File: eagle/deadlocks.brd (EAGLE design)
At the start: 78.7 x 93.3 mm, 18 parts, among them J1 6_PIN_SERIAL_CABLEPTH, U1 328P

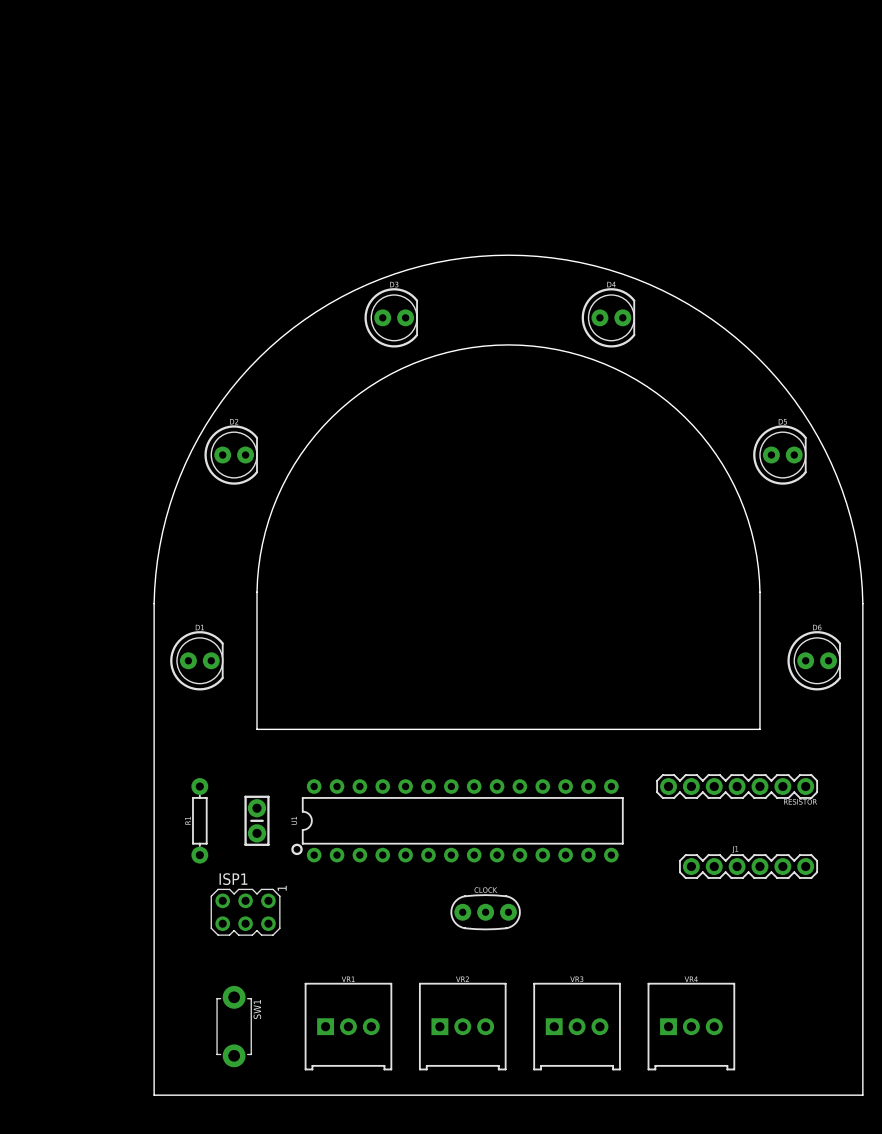
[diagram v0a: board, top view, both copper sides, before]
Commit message: Cleaned up outdated designs and gerbers
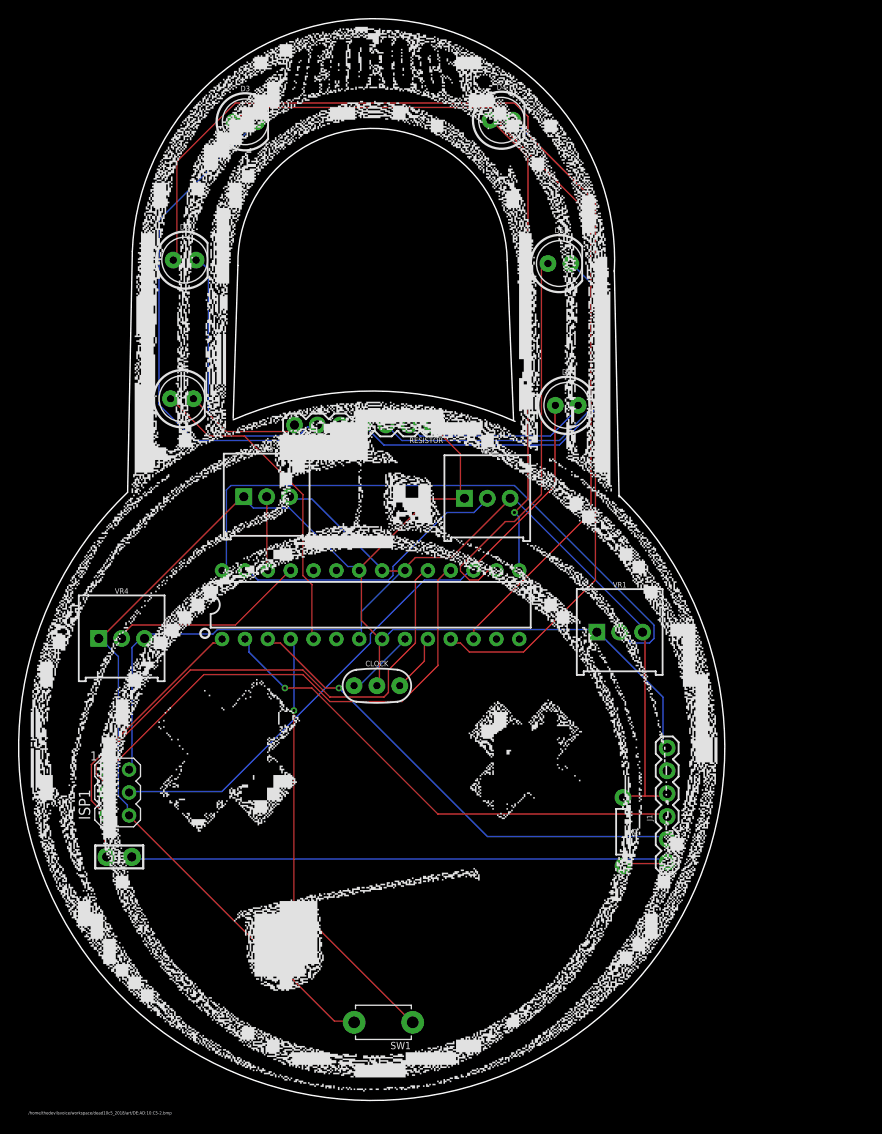
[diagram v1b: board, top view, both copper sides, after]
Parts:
- moved VR4 76.6 mm to (10.4, 52.0)
- moved VR3 68.2 mm to (26.5, 67.8)
- moved VR2 58.8 mm to (51.0, 67.6)
- moved RESISTOR 57.8 mm to (44.8, 75.7)
- moved VR1 53.2 mm to (65.7, 52.7)
- moved R1 47.0 mm to (66.1, 30.5), turned to 270 degrees
- moved D6 39.7 mm to (59.8, 77.9)
- moved D5 32.7 mm to (59.0, 93.7)
- moved D1 29.2 mm to (17.1, 78.6)
- moved CLOCK 27.9 mm to (38.7, 46.8)
- moved D3 27.4 mm to (24.1, 109.4)
- moved U1 26.1 mm to (38.0, 55.8)
- moved D4 25.1 mm to (52.6, 109.6)
- moved D2 22.3 mm to (17.4, 94.0)
- moved ISP1 19.5 mm to (9.91, 34.9), turned to 0 degrees
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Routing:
- net GND: track 0.00 -> 174.4 mm
- net N$20: track 0.00 -> 128.2 mm
- net VCC: track 0.00 -> 126.4 mm
- net N$21: track 0.00 -> 98.6 mm
- net N$18: track 0.00 -> 71.1 mm
- net N$1: track 0.00 -> 69.3 mm
- net N$10: track 0.00 -> 64.8 mm
- net N$14: track 0.00 -> 64.3 mm
- net N$15: track 0.00 -> 58.4 mm
- net N$24: track 0.00 -> 57.4 mm
- net N$8: track 0.00 -> 55.6 mm, vias 0 -> 1
- net N$9: track 0.00 -> 55.4 mm
- net N$7: track 0.00 -> 53.6 mm, vias 0 -> 1
- net N$22: track 0.00 -> 52.6 mm, vias 0 -> 1
- net N$25: track 0.00 -> 48.2 mm, vias 0 -> 1
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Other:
- board size 78.7 x 93.3 mm -> 78.4 x 120.2 mm
- board text added: "/home/thedevilsvoice/workspace/dead10c5_2018/art/DE:AD:10:C5-2.bmp"
- board text added: "@DEAD10C5 DEFCON 26 #Badgelife"
- board text added: "@TheDevilsVoice @mzbat @p0lr_"

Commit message: Re-arranged components, added a power input, and fixed the gerbers so Seeed can manufacture the prototypes.
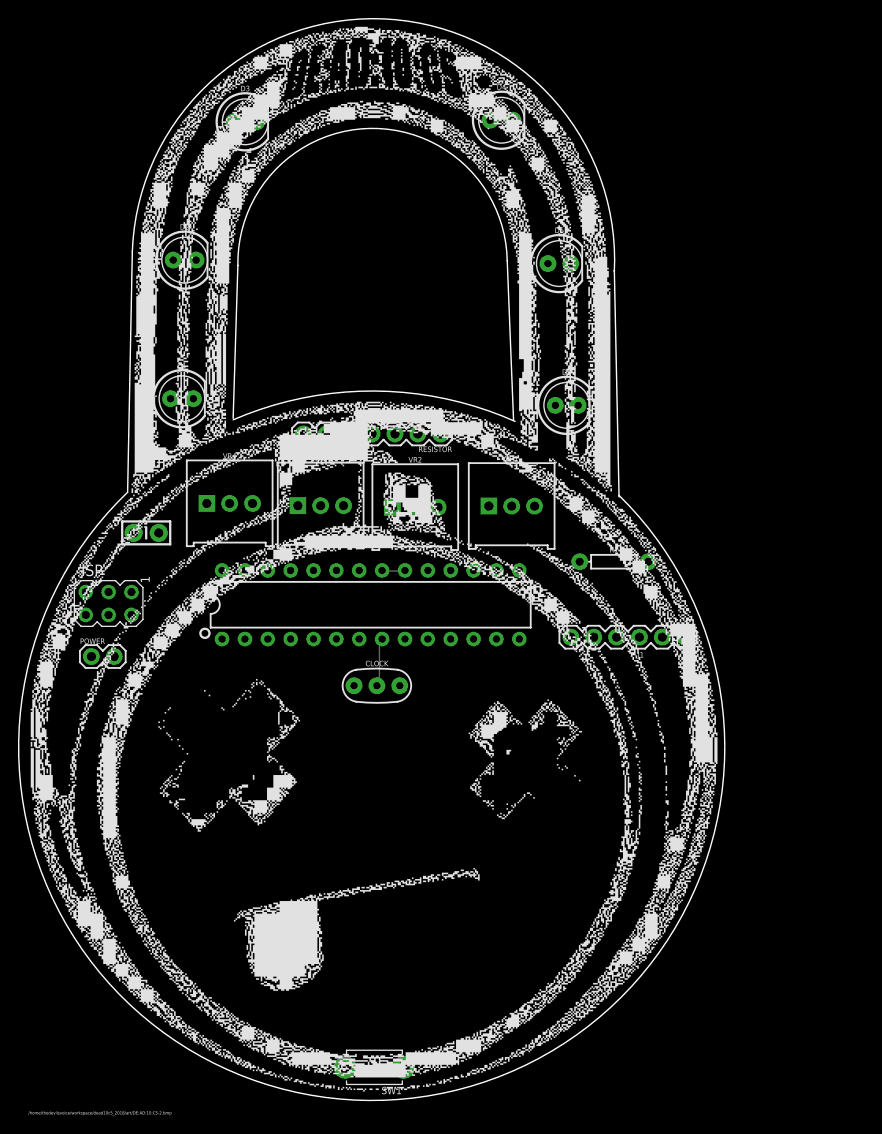
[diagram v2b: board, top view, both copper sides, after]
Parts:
- removed ISP1: AVRISP-6, adafruit:AVRISP
- added ISP: AVRISP-6, adafruit:AVRISP
- added POWER: (no value), SparkFun-Connectors:1X02
- moved C3 36.1 mm to (13.1, 63.7)
- moved R1 30.0 mm to (65.1, 60.5), turned to 0 degrees
- moved J1 25.1 mm to (73.0, 52.1), turned to 180 degrees
- moved VR4 19.2 mm to (22.4, 67.0)
- moved VR1 18.4 mm to (53.7, 66.7)
- moved VR2 8.06 mm to (43.0, 66.6)
- moved VR3 6.08 mm to (32.5, 66.8)
- moved SW1 5.10 mm to (38.4, 4.36)
- moved RESISTOR 1.41 mm to (45.8, 74.7)
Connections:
- net GND: now also ISP.6, POWER.2; no longer ISP1.6
- net N$11: now also ISP.5; no longer ISP1.5
- net N$18: now also ISP.4; no longer ISP1.4
- net N$24: now also ISP.3; no longer ISP1.3
- net N$9: now also ISP.1; no longer ISP1.1
- net VCC: now also ISP.2, POWER.1; no longer ISP1.2
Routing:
- net GND: track 174.4 -> 5.41 mm
- net N$20: track 128.2 -> 0.00 mm
- net VCC: track 126.4 -> 2.56 mm
- net N$21: track 98.6 -> 0.00 mm
- net N$18: track 71.1 -> 0.00 mm
- net N$1: track 69.3 -> 0.00 mm
- net N$10: track 64.8 -> 0.00 mm
- net N$14: track 64.3 -> 0.00 mm
- net N$15: track 58.4 -> 0.00 mm
- net N$24: track 57.4 -> 0.00 mm
- net N$8: track 55.6 -> 0.00 mm, vias 1 -> 0
- net N$9: track 55.4 -> 0.00 mm
- net N$7: track 53.6 -> 0.00 mm, vias 1 -> 0
- net N$22: track 52.6 -> 0.00 mm, vias 1 -> 0
- net N$25: track 48.2 -> 0.00 mm, vias 1 -> 0
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
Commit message: Forgot traces in the last version.
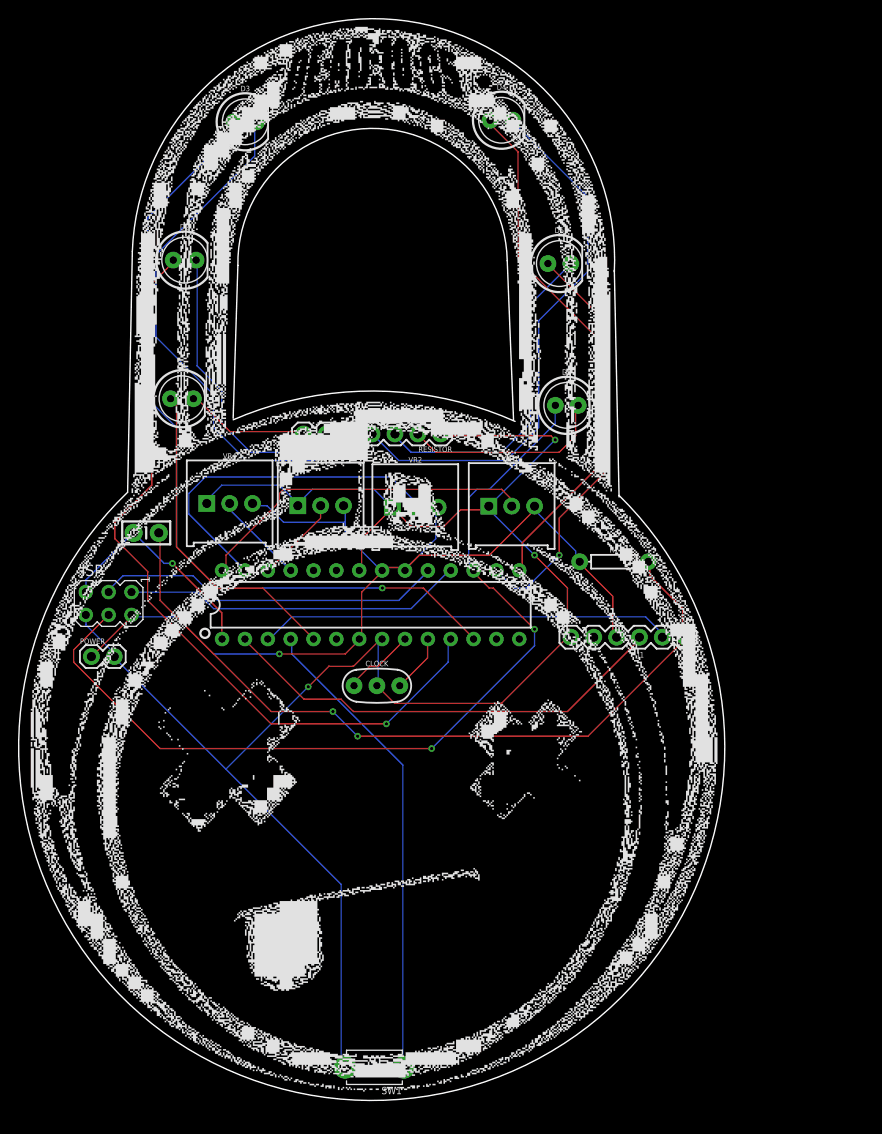
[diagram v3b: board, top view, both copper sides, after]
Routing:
- net GND: track 5.41 -> 204.5 mm, vias 0 -> 3
- net VCC: track 2.56 -> 111.4 mm, vias 0 -> 1
- net N$18: track 0.00 -> 101.6 mm, vias 0 -> 2
- net N$21: track 0.00 -> 89.9 mm, vias 0 -> 1
- net N$10: track 0.00 -> 87.1 mm, vias 0 -> 2
- net N$20: track 0.00 -> 86.6 mm, vias 0 -> 1
- net N$14: track 0.00 -> 61.1 mm
- net N$15: track 0.00 -> 59.2 mm
- net N$22: track 0.00 -> 58.5 mm
- net N$25: track 0.00 -> 52.7 mm
- net N$8: track 0.00 -> 51.1 mm
- net N$23: track 0.00 -> 46.4 mm, vias 0 -> 1
- net N$7: track 0.00 -> 46.0 mm
- net N$4: track 0.00 -> 39.3 mm
- net N$24: track 0.00 -> 38.9 mm
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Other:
- board text removed: "/home/thedevilsvoice/workspace/dead10c5_2018/art/DE:AD:10:C5-2.bmp"

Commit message: A few more mods with new gerbers
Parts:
- removed C3: 0.1uF, SparkFun-Capacitors:CAP-PTH-SMALL-KIT
- added C1: 0.1uF, adafruit:C025-024X044
- RESISTOR: value 10Ohm -> 330 Ohm
- moved CLOCK 23.8 mm to (16.7, 55.8), turned to 90 degrees
- moved R1 1.41 mm to (64.1, 59.5)
- moved ISP 1.00 mm to (8.91, 56.9)
- moved POWER 1.00 mm to (7.00, 51.0), turned to 180 degrees
- moved VR1 1.00 mm to (54.7, 66.7)
- moved VR2 1.00 mm to (44.0, 66.6)
- moved VR3 1.00 mm to (33.5, 66.8)
- turned SW1 to 0 degrees
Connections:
- net N$10: now also C1.1; no longer C3.1
- net N$11: now also C1.2; no longer C3.2
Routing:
- net N$14: track 61.1 -> 99.2 mm
- net N$3: track 6.47 -> 38.0 mm, vias 0 -> 2
- net N$21: track 89.9 -> 114.2 mm, vias 1 -> 0
- net N$2: track 8.08 -> 27.5 mm
- net GND: track 204.5 -> 185.7 mm, vias 3 -> 1
- net N$4: track 39.3 -> 27.4 mm
- net N$10: track 87.1 -> 77.9 mm, vias 2 -> 0
- net N$18: track 101.6 -> 95.3 mm, vias 2 -> 4
- net N$23: track 46.4 -> 41.4 mm, vias 1 -> 0
- net N$20: track 86.6 -> 82.2 mm, vias 1 -> 3
- net VCC: track 111.4 -> 107.2 mm
- net N$7: track 46.0 -> 49.3 mm
- net N$8: track 51.1 -> 48.2 mm
- net N$6: track 10.7 -> 13.5 mm, vias 0 -> 1
- net N$25: track 52.7 -> 50.2 mm
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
